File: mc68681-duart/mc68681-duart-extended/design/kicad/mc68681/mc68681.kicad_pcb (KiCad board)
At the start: 4 copper layers, 80 x 110 mm, 33 parts, among them IC1 XR68C681CJTR-F, IC2 74HCT245, IC3 74HCT245, IC4 74HCT245, IC5 74125, IC6 IC6_DECO.PLD, IC7 IC7_UART_.PLD, J1 Conn_02x32_Odd_Even, J2 EXTBUS, J3 UART_A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

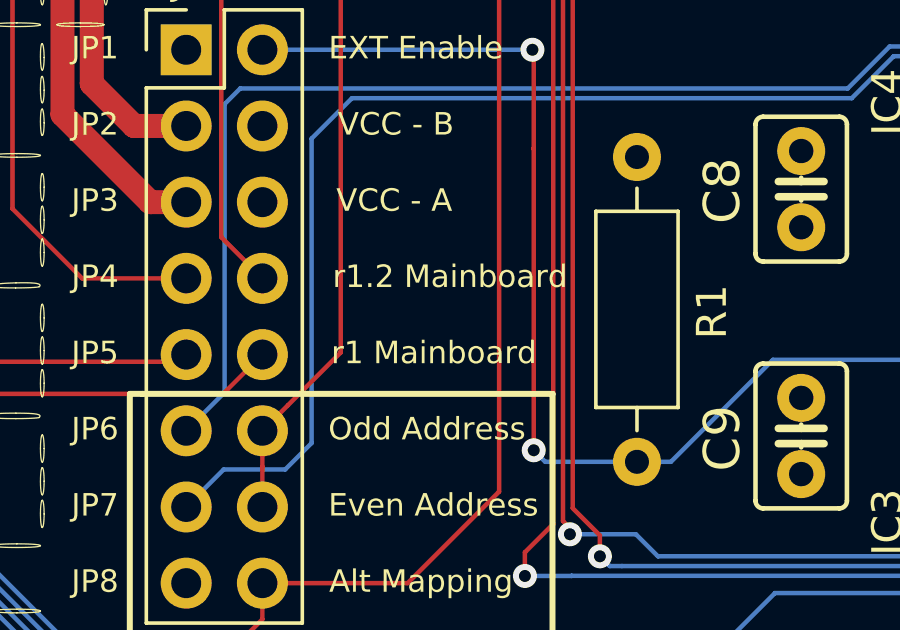
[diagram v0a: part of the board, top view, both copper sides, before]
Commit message: Glue updated and silkscreen fixed
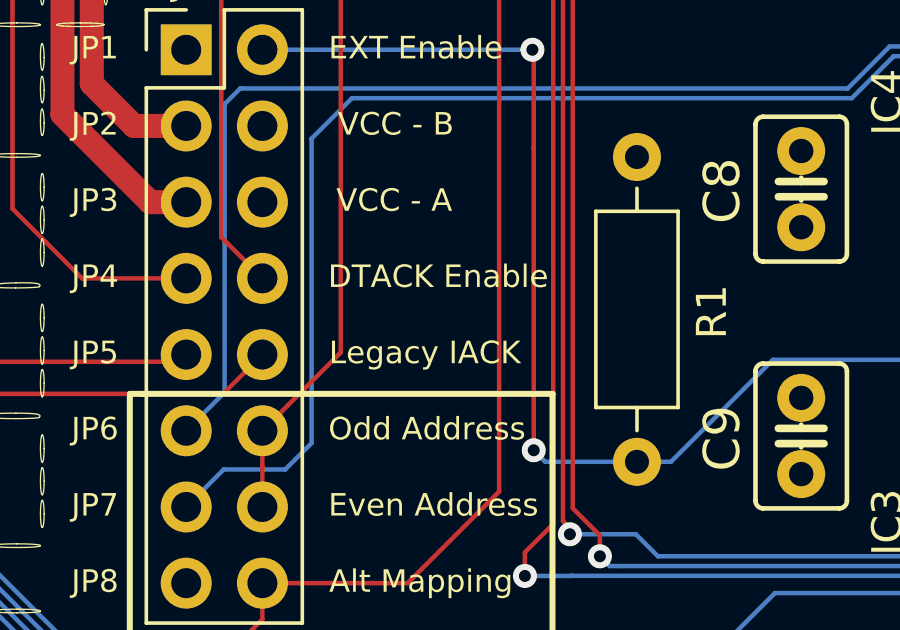
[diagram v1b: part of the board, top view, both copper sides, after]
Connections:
- net JALTA renamed ALTA
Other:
- board text added: "DTACK Enable"
- board text added: "Legacy IACK"
- board text removed: "r1 Mainboard"
- board text removed: "r1.2 Mainboard"
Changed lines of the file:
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@@
   )
   (setup
-    (last_trace_width 0.15)
+    (last_trace_width 0.25)
     (user_trace_width 0.15)
     (user_trace_width 0.4)
@@
   (net 131 LDS)
   (net 132 "Net-(IC6-Pad1)")
-  (net 133 JALTA)
+  (net 133 ALTA)
   (net_class Default "This is the default net class."
     (clearance 0.175)
@@
     (add_net A8)
     (add_net A9)
+    (add_net ALTA)
     (add_net BD0)
     (add_net BD1)
@@
     (add_net IPL2)
     (add_net IRQ)
-    (add_net JALTA)
     (add_net LDS)
     (add_net "Net-(C3-Pad2)")
@@
       (net 1 GND))
     (pad 1 thru_hole circle (at 0 0) (size 1.6 1.6) (drill 0.8) (layers *.Cu *.Mask)
-      (net 133 JALTA))
+      (net 133 ALTA))
     (model ${KISYS3DMOD}/Resistor_THT.3dshapes/R_Axial_DIN0207_L6.3mm_D2.5mm_P10.16mm_Horizontal.wrl
       (at (xyz 0 0 0))
@@
     (fp_line (start 0 -1.27) (end 3.81 -1.27) (layer F.Fab) (width 0.1))
     (pad 16 thru_hole oval (at 2.54 17.78) (size 1.7 1.7) (drill 1) (layers *.Cu *.Mask)
-      (net 133 JALTA))
+      (net 133 ALTA))
     (pad 15 thru_hole oval (at 0 17.78) (size 1.7 1.7) (drill 1) (layers *.Cu *.Mask)
       (net 2 VCC))
@@
       (net 34 A2))
     (pad 17 thru_hole oval (at 7.62 7.62 90) (size 2.4 1.6) (drill 0.8) (layers *.Cu *.Mask)
-      (net 133 JALTA))
+      (net 133 ALTA))
     (pad 7 thru_hole oval (at 0 15.24 90) (size 2.4 1.6) (drill 0.8) (layers *.Cu *.Mask)
       (net 38 A1))
@@
     (effects (font (size 1.8 1.8) (thickness 0.3)))
   )
-  (gr_text "r1 Mainboard" (at 71.257143 143.54) (layer F.SilkS)
+  (gr_text "Legacy IACK" (at 70.953571 143.54) (layer F.SilkS)
     (effects (font (size 0.75 0.75) (thickness 0.15)))
   )
-  (gr_text "r1.2 Mainboard" (at 71.792857 141) (layer F.SilkS)
+  (gr_text "DTACK Enable" (at 71.4 141) (layer F.SilkS)
     (effects (font (size 0.75 0.75) (thickness 0.15)))
   )
@@
   (segment (start 53.19998 52.240019) (end 53.19998 143.10964) (width 0.15) (layer B.Cu) (net 128))
   (segment (start 103.94 51.43) (end 103.94 50.08) (width 0.15) (layer B.Cu) (net 128))
-  (segment (start 62.79 146.86) (end 62.82 146.89) (width 0.15) (layer F.Cu) (net 131))
   (via (at 82.31 92.23) (size 0.8) (drill 0.4) (layers F.Cu B.Cu) (net 129))
   (segment (start 82.27 92.27) (end 82.31 92.23) (width 0.4) (layer F.Cu) (net 129))
@@
   (segment (start 65.54 147.342081) (end 65.54 148.68) (width 0.15) (layer F.Cu) (net 130))
   (segment (start 65.54 146.14) (end 65.54 147.342081) (width 0.15) (layer F.Cu) (net 130))
+  (segment (start 62.79 146.86) (end 62.82 146.89) (width 0.15) (layer F.Cu) (net 131))
   (segment (start 118.46 87) (end 119.73 88.27) (width 0.15) (layer F.Cu) (net 131))
   (segment (start 119.73 88.27) (end 123.06 88.27) (width 0.15) (layer F.Cu) (net 131))

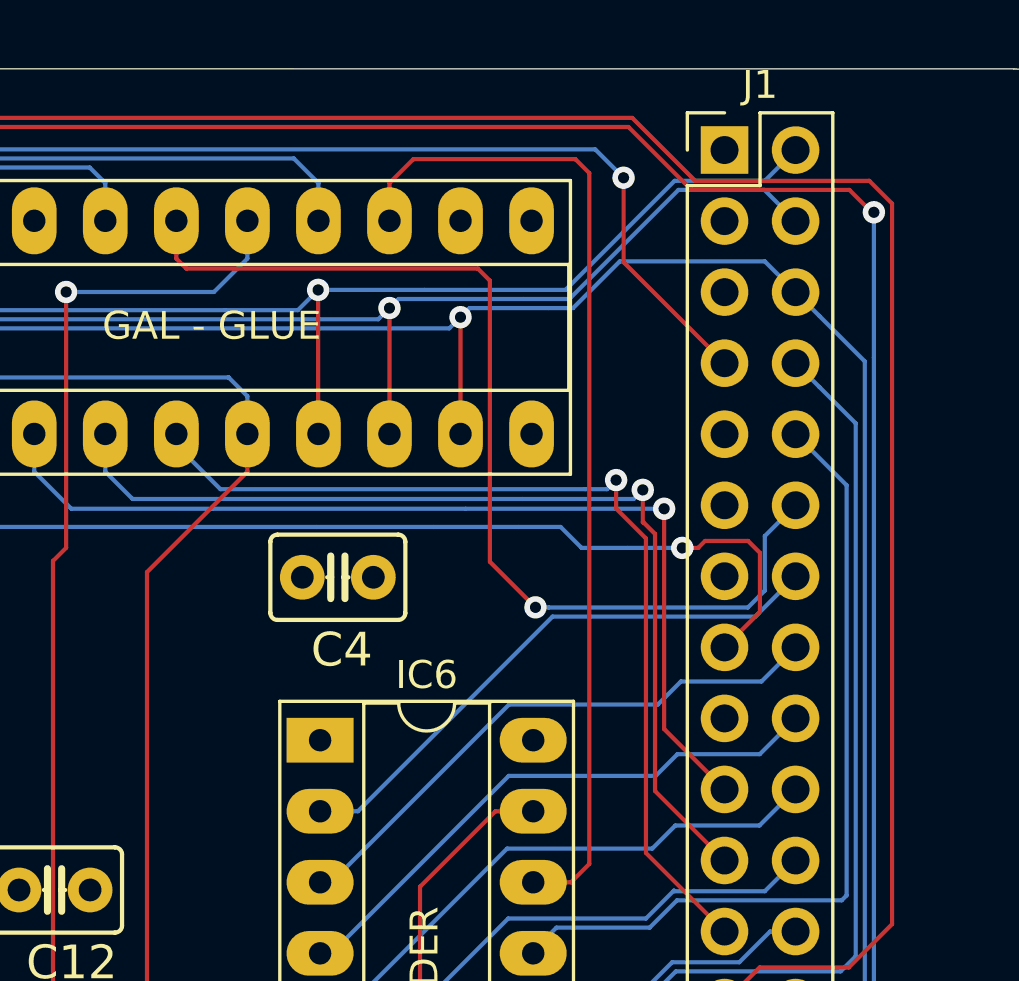
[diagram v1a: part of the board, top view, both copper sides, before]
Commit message: Update for new r2 base address
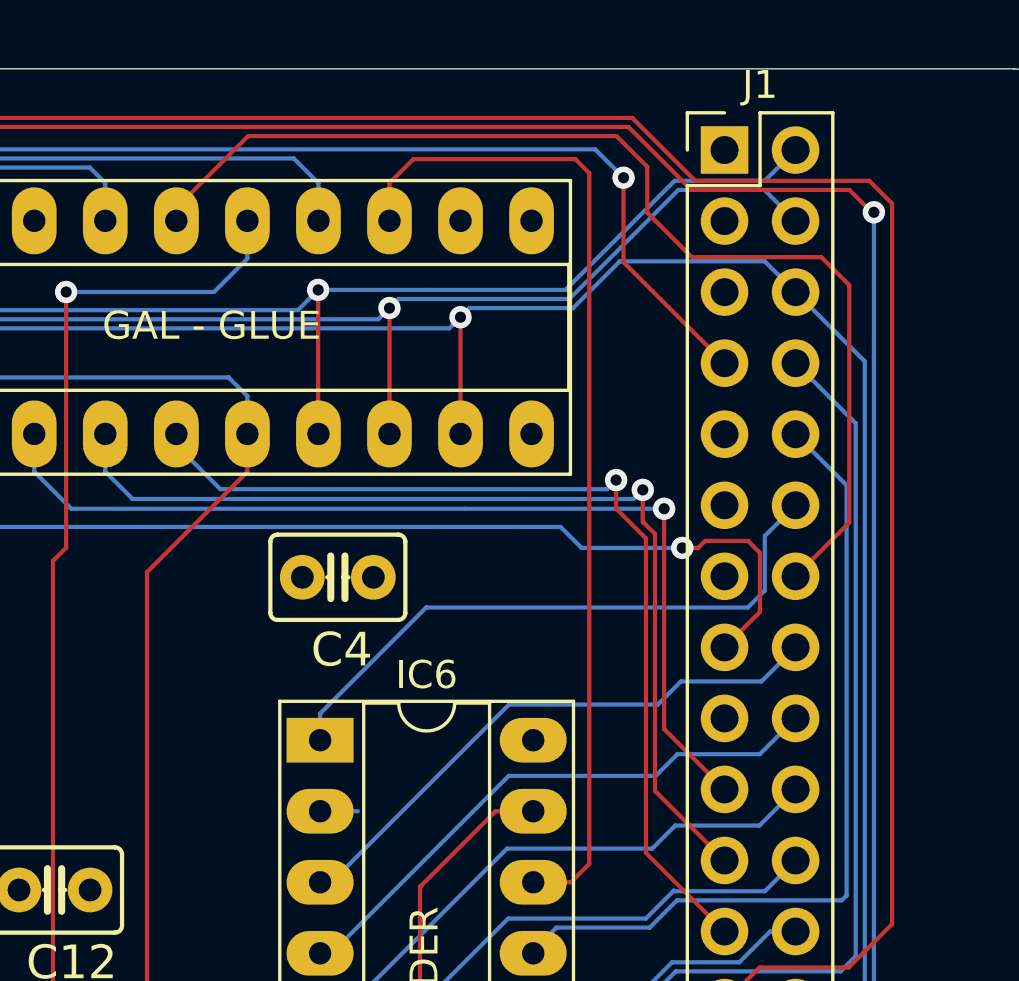
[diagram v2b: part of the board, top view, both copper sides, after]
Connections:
- IC6 pad 1: Net-(IC6-Pad1) -> A6
- IC6 pad 2: A7 -> Net-(IC6-Pad2)
- IC7 pad 16: A6 -> A7
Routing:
- net A7: track 20.5 -> 39.8 mm
- net A6: track 37.2 -> 22.2 mm, vias 1 -> 0
- net Net-(IC6-Pad2): track 0.00 -> 1.35 mm
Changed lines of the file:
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@@
   )
   (setup
-    (last_trace_width 0.25)
+    (last_trace_width 0.15)
     (user_trace_width 0.15)
     (user_trace_width 0.4)
@@
   (net 130 CDS)
   (net 131 LDS)
-  (net 132 "Net-(IC6-Pad1)")
-  (net 133 ALTA)
+  (net 132 ALTA)
+  (net 133 "Net-(IC6-Pad2)")
   (net_class Default "This is the default net class."
     (clearance 0.175)
@@
     (add_net "Net-(IC5-Pad11)")
     (add_net "Net-(IC5-Pad8)")
-    (add_net "Net-(IC6-Pad1)")
     (add_net "Net-(IC6-Pad12)")
+    (add_net "Net-(IC6-Pad2)")
     (add_net "Net-(IC7-Pad11)")
     (add_net "Net-(IC7-Pad12)")
@@
       (net 1 GND))
     (pad 1 thru_hole circle (at 0 0) (size 1.6 1.6) (drill 0.8) (layers *.Cu *.Mask)
-      (net 133 ALTA))
+      (net 132 ALTA))
     (model ${KISYS3DMOD}/Resistor_THT.3dshapes/R_Axial_DIN0207_L6.3mm_D2.5mm_P10.16mm_Horizontal.wrl
       (at (xyz 0 0 0))
@@
     (fp_line (start 0 -1.27) (end 3.81 -1.27) (layer F.Fab) (width 0.1))
     (pad 16 thru_hole oval (at 2.54 17.78) (size 1.7 1.7) (drill 1) (layers *.Cu *.Mask)
-      (net 133 ALTA))
+      (net 132 ALTA))
     (pad 15 thru_hole oval (at 0 17.78) (size 1.7 1.7) (drill 1) (layers *.Cu *.Mask)
       (net 2 VCC))
@@
       (net 34 A2))
     (pad 17 thru_hole oval (at 7.62 7.62 90) (size 2.4 1.6) (drill 0.8) (layers *.Cu *.Mask)
-      (net 133 ALTA))
+      (net 132 ALTA))
     (pad 7 thru_hole oval (at 0 15.24 90) (size 2.4 1.6) (drill 0.8) (layers *.Cu *.Mask)
       (net 38 A1))
     (pad 16 thru_hole oval (at 7.62 10.16 90) (size 2.4 1.6) (drill 0.8) (layers *.Cu *.Mask)
-      (net 72 A6))
+      (net 70 A7))
     (pad 6 thru_hole oval (at 0 12.7 90) (size 2.4 1.6) (drill 0.8) (layers *.Cu *.Mask)
       (net 37 IRQ))
@@
       (net 69 "Net-(IC6-Pad12)"))
     (pad 2 thru_hole oval (at 0 2.54) (size 2.4 1.6) (drill 0.8) (layers *.Cu *.Mask)
-      (net 70 A7))
+      (net 133 "Net-(IC6-Pad2)"))
     (pad 11 thru_hole oval (at 7.62 22.86) (size 2.4 1.6) (drill 0.8) (layers *.Cu *.Mask)
       (net 65 A17))
     (pad 1 thru_hole rect (at 0 0) (size 2.4 1.6) (drill 0.8) (layers *.Cu *.Mask)
-      (net 132 "Net-(IC6-Pad1)"))
+      (net 72 A6))
     (model ${KISYS3DMOD}/Package_DIP.3dshapes/DIP-20_W7.62mm_Socket.wrl
       (at (xyz 0 0 0))
@@
   (segment (start 110.755 68.725) (end 104.4 75.08) (width 0.15) (layer B.Cu) (net 68))
   (segment (start 116.075 68.725) (end 110.755 68.725) (width 0.15) (layer B.Cu) (net 68))
-  (segment (start 112.310001 65.579999) (end 105.35 72.54) (width 0.15) (layer B.Cu) (net 70))
-  (segment (start 119.560001 65.579999) (end 112.310001 65.579999) (width 0.15) (layer B.Cu) (net 70))
-  (segment (start 105.35 72.54) (end 104 72.54) (width 0.15) (layer B.Cu) (net 70))
-  (segment (start 121 64.14) (end 119.560001 65.579999) (width 0.15) (layer B.Cu) (net 70))
+  (segment (start 121 64.14) (end 122.92 62.22) (width 0.15) (layer F.Cu) (net 70))
+  (segment (start 122.92 62.22) (end 122.92 53.73) (width 0.15) (layer F.Cu) (net 70))
+  (segment (start 122.92 53.73) (end 121.92 52.73) (width 0.15) (layer F.Cu) (net 70))
+  (segment (start 121.92 52.73) (end 117.29 52.73) (width 0.15) (layer F.Cu) (net 70))
+  (segment (start 117.29 52.73) (end 115.7 51.14) (width 0.15) (layer F.Cu) (net 70))
+  (segment (start 115.7 49.5) (end 114.60002 48.40002) (width 0.15) (layer F.Cu) (net 70))
+  (segment (start 115.7 51.14) (end 115.7 49.5) (width 0.15) (layer F.Cu) (net 70))
+  (segment (start 101.430347 48.40002) (end 98.630183 51.200184) (width 0.15) (layer F.Cu) (net 70))
+  (segment (start 114.60002 48.40002) (end 101.430347 48.40002) (width 0.15) (layer F.Cu) (net 70))
+  (segment (start 105.35 72.54) (end 104 72.54) (width 0.15) (layer B.Cu) (net 133))
   (segment (start 111.62 85.24) (end 112.19 85.24) (width 0.15) (layer B.Cu) (net 71))
   (segment (start 112.19 85.24) (end 112.7 85.75) (width 0.15) (layer B.Cu) (net 71))
@@
   (segment (start 119.899999 64.650001) (end 119.295011 65.254989) (width 0.15) (layer B.Cu) (net 72))
   (segment (start 121 61.6) (end 119.899999 62.700001) (width 0.15) (layer B.Cu) (net 72))
-  (segment (start 119.295011 65.254989) (end 112.175378 65.254989) (width 0.15) (layer B.Cu) (net 72))
-  (via (at 111.7 65.25) (size 0.8) (drill 0.4) (layers F.Cu B.Cu) (net 72))
-  (segment (start 111.704989 65.254989) (end 111.7 65.25) (width 0.15) (layer B.Cu) (net 72))
-  (segment (start 112.175378 65.254989) (end 111.704989 65.254989) (width 0.15) (layer B.Cu) (net 72))
-  (segment (start 110.07001 63.62001) (end 110.07001 53.56999) (width 0.15) (layer F.Cu) (net 72))
-  (segment (start 111.7 65.25) (end 110.07001 63.62001) (width 0.15) (layer F.Cu) (net 72))
-  (segment (start 110.07001 53.56999) (end 109.64002 53.14) (width 0.15) (layer F.Cu) (net 72))
-  (segment (start 98.86 52.78) (end 98.86 51.43) (width 0.15) (layer F.Cu) (net 72))
-  (segment (start 99.22 53.14) (end 98.86 52.78) (width 0.15) (layer F.Cu) (net 72))
-  (segment (start 109.64002 53.14) (end 99.22 53.14) (width 0.15) (layer F.Cu) (net 72))
+  (segment (start 104 69.05) (end 104 70) (width 0.15) (layer B.Cu) (net 72))
+  (segment (start 107.8 65.25) (end 104 69.05) (width 0.15) (layer B.Cu) (net 72))
+  (segment (start 107.804989 65.254989) (end 107.8 65.25) (width 0.15) (layer B.Cu) (net 72))
+  (segment (start 119.295011 65.254989) (end 107.804989 65.254989) (width 0.15) (layer B.Cu) (net 72))
   (segment (start 98.86 59.45) (end 100.435 61.025) (width 0.15) (layer B.Cu) (net 75))
   (segment (start 98.86 59.05) (end 98.86 59.45) (width 0.15) (layer B.Cu) (net 75))
@@
   (segment (start 86.45 133.33) (end 85.05 134.73) (width 0.15) (layer B.Cu) (net 131))
   (segment (start 124.12 133.33) (end 86.45 133.33) (width 0.15) (layer B.Cu) (net 131))
-  (segment (start 65.54 152.422081) (end 64.742081 153.22) (width 0.15) (layer F.Cu) (net 133))
-  (segment (start 65.54 151.22) (end 65.54 152.422081) (width 0.15) (layer F.Cu) (net 133))
-  (via (at 54.04 153.41) (size 0.8) (drill 0.4) (layers F.Cu B.Cu) (net 133))
-  (segment (start 54.23 153.22) (end 54.04 153.41) (width 0.15) (layer F.Cu) (net 133))
-  (segment (start 64.742081 153.22) (end 54.23 153.22) (width 0.15) (layer F.Cu) (net 133))
-  (segment (start 95.76501 49.52501) (end 96.32 50.08) (width 0.15) (layer B.Cu) (net 133))
-  (segment (start 56.374622 49.52501) (end 95.76501 49.52501) (width 0.15) (layer B.Cu) (net 133))
-  (segment (start 53.52499 52.374642) (end 56.374622 49.52501) (width 0.15) (layer B.Cu) (net 133))
-  (segment (start 96.32 50.08) (end 96.32 51.43) (width 0.15) (layer B.Cu) (net 133))
-  (segment (start 53.52499 152.89499) (end 53.52499 52.374642) (width 0.15) (layer B.Cu) (net 133))
-  (segment (start 54.04 153.41) (end 53.52499 152.89499) (width 0.15) (layer B.Cu) (net 133))
-  (via (at 73.43 126.9) (size 0.8) (drill 0.4) (layers F.Cu B.Cu) (net 133))
-  (segment (start 73.48 126.85) (end 73.43 126.9) (width 0.15) (layer B.Cu) (net 133))
-  (segment (start 79.64 126.85) (end 73.48 126.85) (width 0.15) (layer B.Cu) (net 133))
-  (segment (start 73.43 126.9) (end 73.43 148.17) (width 0.15) (layer F.Cu) (net 133))
-  (segment (start 70.38 151.22) (end 65.54 151.22) (width 0.15) (layer F.Cu) (net 133))
-  (segment (start 73.43 148.17) (end 70.38 151.22) (width 0.15) (layer F.Cu) (net 133))
+  (segment (start 65.54 152.422081) (end 64.742081 153.22) (width 0.15) (layer F.Cu) (net 132))
+  (segment (start 65.54 151.22) (end 65.54 152.422081) (width 0.15) (layer F.Cu) (net 132))
+  (via (at 54.04 153.41) (size 0.8) (drill 0.4) (layers F.Cu B.Cu) (net 132))
+  (segment (start 54.23 153.22) (end 54.04 153.41) (width 0.15) (layer F.Cu) (net 132))
+  (segment (start 64.742081 153.22) (end 54.23 153.22) (width 0.15) (layer F.Cu) (net 132))
+  (segment (start 95.76501 49.52501) (end 96.32 50.08) (width 0.15) (layer B.Cu) (net 132))
+  (segment (start 56.374622 49.52501) (end 95.76501 49.52501) (width 0.15) (layer B.Cu) (net 132))
+  (segment (start 53.52499 52.374642) (end 56.374622 49.52501) (width 0.15) (layer B.Cu) (net 132))
+  (segment (start 96.32 50.08) (end 96.32 51.43) (width 0.15) (layer B.Cu) (net 132))
+  (segment (start 53.52499 152.89499) (end 53.52499 52.374642) (width 0.15) (layer B.Cu) (net 132))
+  (segment (start 54.04 153.41) (end 53.52499 152.89499) (width 0.15) (layer B.Cu) (net 132))
+  (via (at 73.43 126.9) (size 0.8) (drill 0.4) (layers F.Cu B.Cu) (net 132))
+  (segment (start 73.48 126.85) (end 73.43 126.9) (width 0.15) (layer B.Cu) (net 132))
+  (segment (start 79.64 126.85) (end 73.48 126.85) (width 0.15) (layer B.Cu) (net 132))
+  (segment (start 73.43 126.9) (end 73.43 148.17) (width 0.15) (layer F.Cu) (net 132))
+  (segment (start 70.38 151.22) (end 65.54 151.22) (width 0.15) (layer F.Cu) (net 132))
+  (segment (start 73.43 148.17) (end 70.38 151.22) (width 0.15) (layer F.Cu) (net 132))
   (zone (net 1) (net_name GND) (layer In1.Cu) (hatch edge 0.508)
     (connect_pads (clearance 0.508))
